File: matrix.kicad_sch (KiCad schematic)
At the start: 166 parts

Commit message: arcade session 3
added footprints; lots of errors :( problem for next time i am free
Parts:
- D10, D11, D12, D13, D14, D15, D16, D17, D18, D19, D2, D20, D21, D22, D23, D24, D25, D26, D27, D28, D29, D3, D30, D31, D32, D33, D34, D35, D36, D37, D38, D39, D4, D40, D41, D42, D43, D44, D45, D46, D47, D48, D49, D5, D50, D51, D52, D53, D54, D55, D56, D57, D58, D59, D6, D60, D61, D62, D63, D64, D65, D66, D67, D68, D69, D7, D70, D71, D72, D73, D74, D75, D76, D77, D78, D79, D8, D80, D81, D82, D83, D84, D9: footprint (none) -> Diode_SMD:D_SOD-123
- MX29: footprint PCM_marbastlib-mx:SW_MX_HS_CPG151101S11_1u -> PCM_marbastlib-mx:STAB_MX_2u
- MX31, MX44: footprint PCM_marbastlib-mx:SW_MX_HS_CPG151101S11_1u -> PCM_marbastlib-mx:SW_MX_HS_CPG151101S11_1.5u
- MX46, MX71: footprint PCM_marbastlib-mx:SW_MX_HS_CPG151101S11_1u -> PCM_marbastlib-mx:SW_MX_HS_CPG151101S11_1.75u
- MX58, MX60: footprint PCM_marbastlib-mx:SW_MX_HS_CPG151101S11_1u -> PCM_marbastlib-mx:STAB_MX_2.25u
- MX74, MX75, MX76: footprint PCM_marbastlib-mx:SW_MX_HS_CPG151101S11_1u -> PCM_marbastlib-mx:SW_MX_HS_CPG151101S11_1.25u
- MX77: footprint PCM_marbastlib-mx:SW_MX_HS_CPG151101S11_1u -> PCM_marbastlib-mx:STAB_MX_6.25u

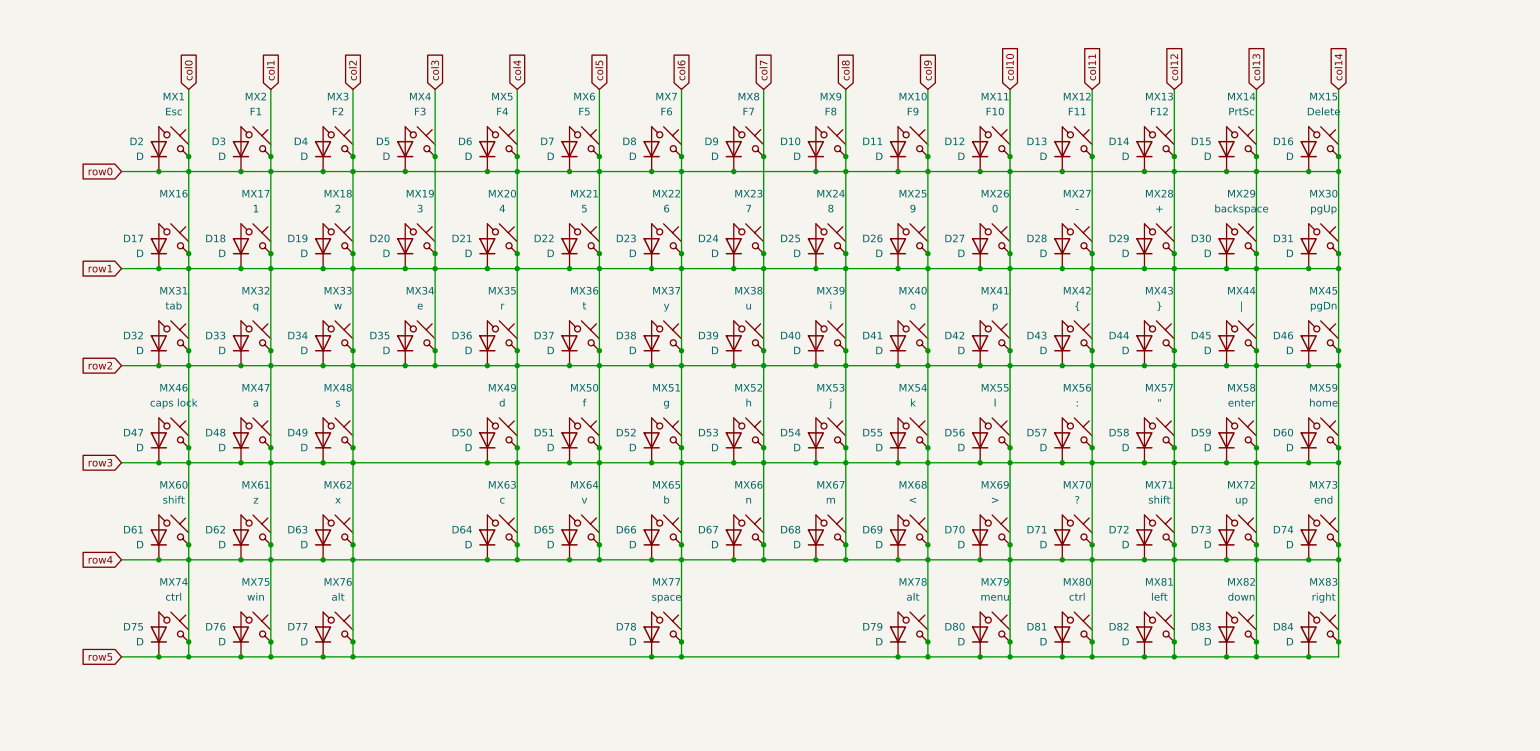
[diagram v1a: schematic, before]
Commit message: arcade session 4(?)
footprints fixed and components placed/pcb editor settings set up
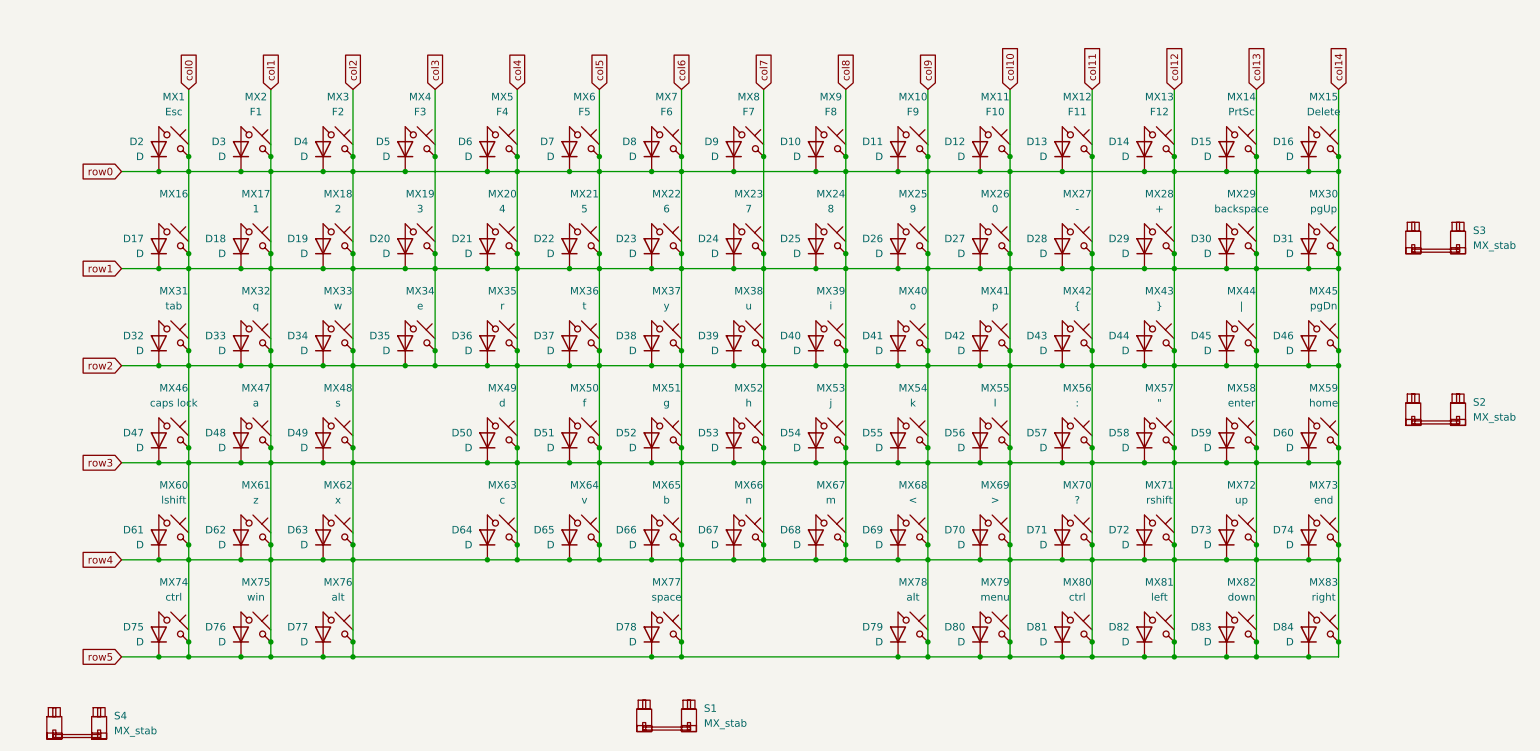
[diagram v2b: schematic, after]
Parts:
- added S1: MX_stab, PCM_marbastlib-mx:STAB_MX_P_6.25u, symbol PCM_marbastlib-mx:MX_stab
- added S2, S4: MX_stab, PCM_marbastlib-mx:STAB_MX_2u, symbol PCM_marbastlib-mx:MX_stab
- added S3: MX_stab, PCM_marbastlib-mx:STAB_MX_P_2u, symbol PCM_marbastlib-mx:MX_stab
- MX29: footprint PCM_marbastlib-mx:STAB_MX_2u -> PCM_marbastlib-mx:SW_MX_HS_CPG151101S11_1u
- MX31, MX44: footprint PCM_marbastlib-mx:SW_MX_HS_CPG151101S11_1.5u -> PCM_marbastlib-mx:SW_MX_HS_CPG151101S11_1u
- MX46: footprint PCM_marbastlib-mx:SW_MX_HS_CPG151101S11_1.75u -> PCM_marbastlib-mx:SW_MX_HS_CPG151101S11_1u
- MX58: footprint PCM_marbastlib-mx:STAB_MX_2.25u -> PCM_marbastlib-mx:SW_MX_HS_CPG151101S11_1u
- MX60: value shift -> lshift; footprint PCM_marbastlib-mx:STAB_MX_2.25u -> PCM_marbastlib-mx:SW_MX_HS_CPG151101S11_1u
- MX71: value shift -> rshift; footprint PCM_marbastlib-mx:SW_MX_HS_CPG151101S11_1.75u -> PCM_marbastlib-mx:SW_MX_HS_CPG151101S11_1u
- MX74, MX75, MX76: footprint PCM_marbastlib-mx:SW_MX_HS_CPG151101S11_1.25u -> PCM_marbastlib-mx:SW_MX_HS_CPG151101S11_1u
- MX77: footprint PCM_marbastlib-mx:STAB_MX_6.25u -> PCM_marbastlib-mx:SW_MX_HS_CPG151101S11_1u

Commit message: fixed mistakes
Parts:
- removed MX1: Esc, PCM_marbastlib-mx:SW_MX_HS_CPG151101S11_1u, symbol PCM_marbastlib-mx:MX_SW_HS_CPG151101S11
- removed MX10: F9, PCM_marbastlib-mx:SW_MX_HS_CPG151101S11_1u, symbol PCM_marbastlib-mx:MX_SW_HS_CPG151101S11
- removed MX11: F10, PCM_marbastlib-mx:SW_MX_HS_CPG151101S11_1u, symbol PCM_marbastlib-mx:MX_SW_HS_CPG151101S11
- removed MX12: F11, PCM_marbastlib-mx:SW_MX_HS_CPG151101S11_1u, symbol PCM_marbastlib-mx:MX_SW_HS_CPG151101S11
- removed MX13: F12, PCM_marbastlib-mx:SW_MX_HS_CPG151101S11_1u, symbol PCM_marbastlib-mx:MX_SW_HS_CPG151101S11
- removed MX14: PrtSc, PCM_marbastlib-mx:SW_MX_HS_CPG151101S11_1u, symbol PCM_marbastlib-mx:MX_SW_HS_CPG151101S11
- removed MX15: Delete, PCM_marbastlib-mx:SW_MX_HS_CPG151101S11_1u, symbol PCM_marbastlib-mx:MX_SW_HS_CPG151101S11
- removed MX16: ~, PCM_marbastlib-mx:SW_MX_HS_CPG151101S11_1u, symbol PCM_marbastlib-mx:MX_SW_HS_CPG151101S11
- removed MX17: 1, PCM_marbastlib-mx:SW_MX_HS_CPG151101S11_1u, symbol PCM_marbastlib-mx:MX_SW_HS_CPG151101S11
- removed MX18: 2, PCM_marbastlib-mx:SW_MX_HS_CPG151101S11_1u, symbol PCM_marbastlib-mx:MX_SW_HS_CPG151101S11
- removed MX19: 3, PCM_marbastlib-mx:SW_MX_HS_CPG151101S11_1u, symbol PCM_marbastlib-mx:MX_SW_HS_CPG151101S11
- removed MX2: F1, PCM_marbastlib-mx:SW_MX_HS_CPG151101S11_1u, symbol PCM_marbastlib-mx:MX_SW_HS_CPG151101S11
- removed MX20: 4, PCM_marbastlib-mx:SW_MX_HS_CPG151101S11_1u, symbol PCM_marbastlib-mx:MX_SW_HS_CPG151101S11
- removed MX21: 5, PCM_marbastlib-mx:SW_MX_HS_CPG151101S11_1u, symbol PCM_marbastlib-mx:MX_SW_HS_CPG151101S11
- removed MX22: 6, PCM_marbastlib-mx:SW_MX_HS_CPG151101S11_1u, symbol PCM_marbastlib-mx:MX_SW_HS_CPG151101S11
- removed MX23: 7, PCM_marbastlib-mx:SW_MX_HS_CPG151101S11_1u, symbol PCM_marbastlib-mx:MX_SW_HS_CPG151101S11
- removed MX24: 8, PCM_marbastlib-mx:SW_MX_HS_CPG151101S11_1u, symbol PCM_marbastlib-mx:MX_SW_HS_CPG151101S11
- removed MX25: 9, PCM_marbastlib-mx:SW_MX_HS_CPG151101S11_1u, symbol PCM_marbastlib-mx:MX_SW_HS_CPG151101S11
- removed MX26: 0, PCM_marbastlib-mx:SW_MX_HS_CPG151101S11_1u, symbol PCM_marbastlib-mx:MX_SW_HS_CPG151101S11
- removed MX27: -, PCM_marbastlib-mx:SW_MX_HS_CPG151101S11_1u, symbol PCM_marbastlib-mx:MX_SW_HS_CPG151101S11
- removed MX28: +, PCM_marbastlib-mx:SW_MX_HS_CPG151101S11_1u, symbol PCM_marbastlib-mx:MX_SW_HS_CPG151101S11
- removed MX29: backspace, PCM_marbastlib-mx:SW_MX_HS_CPG151101S11_1u, symbol PCM_marbastlib-mx:MX_SW_HS_CPG151101S11
- removed MX3: F2, PCM_marbastlib-mx:SW_MX_HS_CPG151101S11_1u, symbol PCM_marbastlib-mx:MX_SW_HS_CPG151101S11
- removed MX30: pgUp, PCM_marbastlib-mx:SW_MX_HS_CPG151101S11_1u, symbol PCM_marbastlib-mx:MX_SW_HS_CPG151101S11
- removed MX31: tab, PCM_marbastlib-mx:SW_MX_HS_CPG151101S11_1u, symbol PCM_marbastlib-mx:MX_SW_HS_CPG151101S11
- removed MX32: q, PCM_marbastlib-mx:SW_MX_HS_CPG151101S11_1u, symbol PCM_marbastlib-mx:MX_SW_HS_CPG151101S11
- removed MX33: w, PCM_marbastlib-mx:SW_MX_HS_CPG151101S11_1u, symbol PCM_marbastlib-mx:MX_SW_HS_CPG151101S11
- removed MX34: e, PCM_marbastlib-mx:SW_MX_HS_CPG151101S11_1u, symbol PCM_marbastlib-mx:MX_SW_HS_CPG151101S11
- removed MX35: r, PCM_marbastlib-mx:SW_MX_HS_CPG151101S11_1u, symbol PCM_marbastlib-mx:MX_SW_HS_CPG151101S11
- removed MX36: t, PCM_marbastlib-mx:SW_MX_HS_CPG151101S11_1u, symbol PCM_marbastlib-mx:MX_SW_HS_CPG151101S11
- removed MX37: y, PCM_marbastlib-mx:SW_MX_HS_CPG151101S11_1u, symbol PCM_marbastlib-mx:MX_SW_HS_CPG151101S11
- removed MX38: u, PCM_marbastlib-mx:SW_MX_HS_CPG151101S11_1u, symbol PCM_marbastlib-mx:MX_SW_HS_CPG151101S11
- removed MX39: i, PCM_marbastlib-mx:SW_MX_HS_CPG151101S11_1u, symbol PCM_marbastlib-mx:MX_SW_HS_CPG151101S11
- removed MX4: F3, PCM_marbastlib-mx:SW_MX_HS_CPG151101S11_1u, symbol PCM_marbastlib-mx:MX_SW_HS_CPG151101S11
- removed MX40: o, PCM_marbastlib-mx:SW_MX_HS_CPG151101S11_1u, symbol PCM_marbastlib-mx:MX_SW_HS_CPG151101S11
- removed MX41: p, PCM_marbastlib-mx:SW_MX_HS_CPG151101S11_1u, symbol PCM_marbastlib-mx:MX_SW_HS_CPG151101S11
- removed MX42: {, PCM_marbastlib-mx:SW_MX_HS_CPG151101S11_1u, symbol PCM_marbastlib-mx:MX_SW_HS_CPG151101S11
- removed MX43: }, PCM_marbastlib-mx:SW_MX_HS_CPG151101S11_1u, symbol PCM_marbastlib-mx:MX_SW_HS_CPG151101S11
- removed MX44: |, PCM_marbastlib-mx:SW_MX_HS_CPG151101S11_1u, symbol PCM_marbastlib-mx:MX_SW_HS_CPG151101S11
- removed MX45: pgDn, PCM_marbastlib-mx:SW_MX_HS_CPG151101S11_1u, symbol PCM_marbastlib-mx:MX_SW_HS_CPG151101S11
- removed MX46: caps lock, PCM_marbastlib-mx:SW_MX_HS_CPG151101S11_1u, symbol PCM_marbastlib-mx:MX_SW_HS_CPG151101S11
- removed MX47: a, PCM_marbastlib-mx:SW_MX_HS_CPG151101S11_1u, symbol PCM_marbastlib-mx:MX_SW_HS_CPG151101S11
- removed MX48: s, PCM_marbastlib-mx:SW_MX_HS_CPG151101S11_1u, symbol PCM_marbastlib-mx:MX_SW_HS_CPG151101S11
- removed MX49: d, PCM_marbastlib-mx:SW_MX_HS_CPG151101S11_1u, symbol PCM_marbastlib-mx:MX_SW_HS_CPG151101S11
- removed MX5: F4, PCM_marbastlib-mx:SW_MX_HS_CPG151101S11_1u, symbol PCM_marbastlib-mx:MX_SW_HS_CPG151101S11
- removed MX50: f, PCM_marbastlib-mx:SW_MX_HS_CPG151101S11_1u, symbol PCM_marbastlib-mx:MX_SW_HS_CPG151101S11
- removed MX51: g, PCM_marbastlib-mx:SW_MX_HS_CPG151101S11_1u, symbol PCM_marbastlib-mx:MX_SW_HS_CPG151101S11
- removed MX52: h, PCM_marbastlib-mx:SW_MX_HS_CPG151101S11_1u, symbol PCM_marbastlib-mx:MX_SW_HS_CPG151101S11
- removed MX53: j, PCM_marbastlib-mx:SW_MX_HS_CPG151101S11_1u, symbol PCM_marbastlib-mx:MX_SW_HS_CPG151101S11
- removed MX54: k, PCM_marbastlib-mx:SW_MX_HS_CPG151101S11_1u, symbol PCM_marbastlib-mx:MX_SW_HS_CPG151101S11
- removed MX55: l, PCM_marbastlib-mx:SW_MX_HS_CPG151101S11_1u, symbol PCM_marbastlib-mx:MX_SW_HS_CPG151101S11
- removed MX56: :, PCM_marbastlib-mx:SW_MX_HS_CPG151101S11_1u, symbol PCM_marbastlib-mx:MX_SW_HS_CPG151101S11
- removed MX57: ", PCM_marbastlib-mx:SW_MX_HS_CPG151101S11_1u, symbol PCM_marbastlib-mx:MX_SW_HS_CPG151101S11
- removed MX58: enter, PCM_marbastlib-mx:SW_MX_HS_CPG151101S11_1u, symbol PCM_marbastlib-mx:MX_SW_HS_CPG151101S11
- removed MX59: home, PCM_marbastlib-mx:SW_MX_HS_CPG151101S11_1u, symbol PCM_marbastlib-mx:MX_SW_HS_CPG151101S11
- removed MX6: F5, PCM_marbastlib-mx:SW_MX_HS_CPG151101S11_1u, symbol PCM_marbastlib-mx:MX_SW_HS_CPG151101S11
- removed MX60: lshift, PCM_marbastlib-mx:SW_MX_HS_CPG151101S11_1u, symbol PCM_marbastlib-mx:MX_SW_HS_CPG151101S11
- removed MX61: z, PCM_marbastlib-mx:SW_MX_HS_CPG151101S11_1u, symbol PCM_marbastlib-mx:MX_SW_HS_CPG151101S11
- removed MX62: x, PCM_marbastlib-mx:SW_MX_HS_CPG151101S11_1u, symbol PCM_marbastlib-mx:MX_SW_HS_CPG151101S11
- removed MX63: c, PCM_marbastlib-mx:SW_MX_HS_CPG151101S11_1u, symbol PCM_marbastlib-mx:MX_SW_HS_CPG151101S11
- removed MX64: v, PCM_marbastlib-mx:SW_MX_HS_CPG151101S11_1u, symbol PCM_marbastlib-mx:MX_SW_HS_CPG151101S11
- removed MX65: b, PCM_marbastlib-mx:SW_MX_HS_CPG151101S11_1u, symbol PCM_marbastlib-mx:MX_SW_HS_CPG151101S11
- removed MX66: n, PCM_marbastlib-mx:SW_MX_HS_CPG151101S11_1u, symbol PCM_marbastlib-mx:MX_SW_HS_CPG151101S11
- removed MX67: m, PCM_marbastlib-mx:SW_MX_HS_CPG151101S11_1u, symbol PCM_marbastlib-mx:MX_SW_HS_CPG151101S11
- removed MX68: <, PCM_marbastlib-mx:SW_MX_HS_CPG151101S11_1u, symbol PCM_marbastlib-mx:MX_SW_HS_CPG151101S11
- removed MX69: >, PCM_marbastlib-mx:SW_MX_HS_CPG151101S11_1u, symbol PCM_marbastlib-mx:MX_SW_HS_CPG151101S11
- removed MX7: F6, PCM_marbastlib-mx:SW_MX_HS_CPG151101S11_1u, symbol PCM_marbastlib-mx:MX_SW_HS_CPG151101S11
- removed MX70: ?, PCM_marbastlib-mx:SW_MX_HS_CPG151101S11_1u, symbol PCM_marbastlib-mx:MX_SW_HS_CPG151101S11
- removed MX71: rshift, PCM_marbastlib-mx:SW_MX_HS_CPG151101S11_1u, symbol PCM_marbastlib-mx:MX_SW_HS_CPG151101S11
- removed MX72: up, PCM_marbastlib-mx:SW_MX_HS_CPG151101S11_1u, symbol PCM_marbastlib-mx:MX_SW_HS_CPG151101S11
- removed MX73: end, PCM_marbastlib-mx:SW_MX_HS_CPG151101S11_1u, symbol PCM_marbastlib-mx:MX_SW_HS_CPG151101S11
- removed MX74, MX80: ctrl, PCM_marbastlib-mx:SW_MX_HS_CPG151101S11_1u, symbol PCM_marbastlib-mx:MX_SW_HS_CPG151101S11
- removed MX75: win, PCM_marbastlib-mx:SW_MX_HS_CPG151101S11_1u, symbol PCM_marbastlib-mx:MX_SW_HS_CPG151101S11
- removed MX76, MX78: alt, PCM_marbastlib-mx:SW_MX_HS_CPG151101S11_1u, symbol PCM_marbastlib-mx:MX_SW_HS_CPG151101S11
- removed MX77: space, PCM_marbastlib-mx:SW_MX_HS_CPG151101S11_1u, symbol PCM_marbastlib-mx:MX_SW_HS_CPG151101S11
- removed MX79: menu, PCM_marbastlib-mx:SW_MX_HS_CPG151101S11_1u, symbol PCM_marbastlib-mx:MX_SW_HS_CPG151101S11
- removed MX8: F7, PCM_marbastlib-mx:SW_MX_HS_CPG151101S11_1u, symbol PCM_marbastlib-mx:MX_SW_HS_CPG151101S11
- removed MX81: left, PCM_marbastlib-mx:SW_MX_HS_CPG151101S11_1u, symbol PCM_marbastlib-mx:MX_SW_HS_CPG151101S11
- removed MX82: down, PCM_marbastlib-mx:SW_MX_HS_CPG151101S11_1u, symbol PCM_marbastlib-mx:MX_SW_HS_CPG151101S11
- removed MX83: right, PCM_marbastlib-mx:SW_MX_HS_CPG151101S11_1u, symbol PCM_marbastlib-mx:MX_SW_HS_CPG151101S11
- removed MX9: F8, PCM_marbastlib-mx:SW_MX_HS_CPG151101S11_1u, symbol PCM_marbastlib-mx:MX_SW_HS_CPG151101S11
- removed S1: MX_stab, PCM_marbastlib-mx:STAB_MX_P_6.25u, symbol PCM_marbastlib-mx:MX_stab
- removed S2, S4: MX_stab, PCM_marbastlib-mx:STAB_MX_2u, symbol PCM_marbastlib-mx:MX_stab
- removed S3: MX_stab, PCM_marbastlib-mx:STAB_MX_P_2u, symbol PCM_marbastlib-mx:MX_stab
- added MX1: esc, MX_Alps_Hybrid:MX-Alps-Hybrid-1U, symbol PCM_marbastlib-mx:MX_SW_solder
- added MX10: f9, MX_Alps_Hybrid:MX-Alps-Hybrid-1U, symbol PCM_marbastlib-mx:MX_SW_solder
- added MX11: f10, MX_Alps_Hybrid:MX-Alps-Hybrid-1U, symbol PCM_marbastlib-mx:MX_SW_solder
- added MX12: f11, MX_Alps_Hybrid:MX-Alps-Hybrid-1U, symbol PCM_marbastlib-mx:MX_SW_solder
- added MX13: f12, MX_Alps_Hybrid:MX-Alps-Hybrid-1U, symbol PCM_marbastlib-mx:MX_SW_solder
- added MX14: prtsc, MX_Alps_Hybrid:MX-Alps-Hybrid-1U, symbol PCM_marbastlib-mx:MX_SW_solder
- added MX15: del, MX_Alps_Hybrid:MX-Alps-Hybrid-1U, symbol PCM_marbastlib-mx:MX_SW_solder
- added MX16: ~, MX_Alps_Hybrid:MX-Alps-Hybrid-1U, symbol PCM_marbastlib-mx:MX_SW_solder
- added MX17: 1, MX_Alps_Hybrid:MX-Alps-Hybrid-1U, symbol PCM_marbastlib-mx:MX_SW_solder
- added MX18: 2, MX_Alps_Hybrid:MX-Alps-Hybrid-1U, symbol PCM_marbastlib-mx:MX_SW_solder
- added MX19: 3, MX_Alps_Hybrid:MX-Alps-Hybrid-1U, symbol PCM_marbastlib-mx:MX_SW_solder
- added MX2: f1, MX_Alps_Hybrid:MX-Alps-Hybrid-1U, symbol PCM_marbastlib-mx:MX_SW_solder
- added MX20: 4, MX_Alps_Hybrid:MX-Alps-Hybrid-1U, symbol PCM_marbastlib-mx:MX_SW_solder
- added MX21: 5, MX_Alps_Hybrid:MX-Alps-Hybrid-1U, symbol PCM_marbastlib-mx:MX_SW_solder
- added MX22: 6, MX_Alps_Hybrid:MX-Alps-Hybrid-1U, symbol PCM_marbastlib-mx:MX_SW_solder
- added MX23: 7, MX_Alps_Hybrid:MX-Alps-Hybrid-1U, symbol PCM_marbastlib-mx:MX_SW_solder
- added MX24: 8, MX_Alps_Hybrid:MX-Alps-Hybrid-1U, symbol PCM_marbastlib-mx:MX_SW_solder
- added MX25: 9, MX_Alps_Hybrid:MX-Alps-Hybrid-1U, symbol PCM_marbastlib-mx:MX_SW_solder
- added MX26: 0, MX_Alps_Hybrid:MX-Alps-Hybrid-1U, symbol PCM_marbastlib-mx:MX_SW_solder
- added MX27: -, MX_Alps_Hybrid:MX-Alps-Hybrid-1U, symbol PCM_marbastlib-mx:MX_SW_solder
- added MX28: =, MX_Alps_Hybrid:MX-Alps-Hybrid-1U, symbol PCM_marbastlib-mx:MX_SW_solder
- added MX29: backspace, MX_Alps_Hybrid:MX-Alps-Hybrid-2U-ReversedStabilizers, symbol PCM_marbastlib-mx:MX_SW_solder
- added MX3: f2, MX_Alps_Hybrid:MX-Alps-Hybrid-1U, symbol PCM_marbastlib-mx:MX_SW_solder
- added MX30: pgup, MX_Alps_Hybrid:MX-Alps-Hybrid-1U, symbol PCM_marbastlib-mx:MX_SW_solder
- added MX31: tab, MX_Alps_Hybrid:MX-Alps-Hybrid-1.5U, symbol PCM_marbastlib-mx:MX_SW_solder
- added MX32: q, MX_Alps_Hybrid:MX-Alps-Hybrid-1U, symbol PCM_marbastlib-mx:MX_SW_solder
- added MX33: w, MX_Alps_Hybrid:MX-Alps-Hybrid-1U, symbol PCM_marbastlib-mx:MX_SW_solder
- added MX34: e, MX_Alps_Hybrid:MX-Alps-Hybrid-1U, symbol PCM_marbastlib-mx:MX_SW_solder
- added MX35: r, MX_Alps_Hybrid:MX-Alps-Hybrid-1U, symbol PCM_marbastlib-mx:MX_SW_solder
- added MX36: t, MX_Alps_Hybrid:MX-Alps-Hybrid-1U, symbol PCM_marbastlib-mx:MX_SW_solder
- added MX37: y, MX_Alps_Hybrid:MX-Alps-Hybrid-1U, symbol PCM_marbastlib-mx:MX_SW_solder
- added MX38: u, MX_Alps_Hybrid:MX-Alps-Hybrid-1U, symbol PCM_marbastlib-mx:MX_SW_solder
- added MX39: i, MX_Alps_Hybrid:MX-Alps-Hybrid-1U, symbol PCM_marbastlib-mx:MX_SW_solder
- added MX4: f3, MX_Alps_Hybrid:MX-Alps-Hybrid-1U, symbol PCM_marbastlib-mx:MX_SW_solder
- added MX40: o, MX_Alps_Hybrid:MX-Alps-Hybrid-1U, symbol PCM_marbastlib-mx:MX_SW_solder
- added MX41: p, MX_Alps_Hybrid:MX-Alps-Hybrid-1U, symbol PCM_marbastlib-mx:MX_SW_solder
- added MX42: [, MX_Alps_Hybrid:MX-Alps-Hybrid-1U, symbol PCM_marbastlib-mx:MX_SW_solder
- added MX43: ], MX_Alps_Hybrid:MX-Alps-Hybrid-1U, symbol PCM_marbastlib-mx:MX_SW_solder
- added MX44: \, MX_Alps_Hybrid:MX-Alps-Hybrid-1.5U, symbol PCM_marbastlib-mx:MX_SW_solder
- added MX45: pgdn, MX_Alps_Hybrid:MX-Alps-Hybrid-1U, symbol PCM_marbastlib-mx:MX_SW_solder
- added MX46: caps lock, MX_Alps_Hybrid:MX-Alps-Hybrid-1.75U, symbol PCM_marbastlib-mx:MX_SW_solder
- added MX47: a, MX_Alps_Hybrid:MX-Alps-Hybrid-1U, symbol PCM_marbastlib-mx:MX_SW_solder
- added MX48: s, MX_Alps_Hybrid:MX-Alps-Hybrid-1U, symbol PCM_marbastlib-mx:MX_SW_solder
- added MX49: d, MX_Alps_Hybrid:MX-Alps-Hybrid-1U, symbol PCM_marbastlib-mx:MX_SW_solder
- added MX5: f4, MX_Alps_Hybrid:MX-Alps-Hybrid-1U, symbol PCM_marbastlib-mx:MX_SW_solder
- added MX50: f, MX_Alps_Hybrid:MX-Alps-Hybrid-1U, symbol PCM_marbastlib-mx:MX_SW_solder
- added MX51: g, MX_Alps_Hybrid:MX-Alps-Hybrid-1U, symbol PCM_marbastlib-mx:MX_SW_solder
- added MX52: h, MX_Alps_Hybrid:MX-Alps-Hybrid-1U, symbol PCM_marbastlib-mx:MX_SW_solder
- added MX53: j, MX_Alps_Hybrid:MX-Alps-Hybrid-1U, symbol PCM_marbastlib-mx:MX_SW_solder
- added MX54: k, MX_Alps_Hybrid:MX-Alps-Hybrid-1U, symbol PCM_marbastlib-mx:MX_SW_solder
- added MX55: l, MX_Alps_Hybrid:MX-Alps-Hybrid-1U, symbol PCM_marbastlib-mx:MX_SW_solder
- added MX56: ;, MX_Alps_Hybrid:MX-Alps-Hybrid-1U, symbol PCM_marbastlib-mx:MX_SW_solder
- added MX57: ', MX_Alps_Hybrid:MX-Alps-Hybrid-1U, symbol PCM_marbastlib-mx:MX_SW_solder
- added MX58: enter, MX_Alps_Hybrid:MX-Alps-Hybrid-2.25U-ReversedStabilizers, symbol PCM_marbastlib-mx:MX_SW_solder
- added MX59: home, MX_Alps_Hybrid:MX-Alps-Hybrid-1U, symbol PCM_marbastlib-mx:MX_SW_solder
- added MX6: f5, MX_Alps_Hybrid:MX-Alps-Hybrid-1U, symbol PCM_marbastlib-mx:MX_SW_solder
- added MX60: lshift, MX_Alps_Hybrid:MX-Alps-Hybrid-2.25U-ReversedStabilizers, symbol PCM_marbastlib-mx:MX_SW_solder
- added MX61: z, MX_Alps_Hybrid:MX-Alps-Hybrid-1U, symbol PCM_marbastlib-mx:MX_SW_solder
- added MX62: x, MX_Alps_Hybrid:MX-Alps-Hybrid-1U, symbol PCM_marbastlib-mx:MX_SW_solder
- added MX63: c, MX_Alps_Hybrid:MX-Alps-Hybrid-1U, symbol PCM_marbastlib-mx:MX_SW_solder
- added MX64: v, MX_Alps_Hybrid:MX-Alps-Hybrid-1U, symbol PCM_marbastlib-mx:MX_SW_solder
- added MX65: b, MX_Alps_Hybrid:MX-Alps-Hybrid-1U, symbol PCM_marbastlib-mx:MX_SW_solder
- added MX66: n, MX_Alps_Hybrid:MX-Alps-Hybrid-1U, symbol PCM_marbastlib-mx:MX_SW_solder
- added MX67: m, MX_Alps_Hybrid:MX-Alps-Hybrid-1U, symbol PCM_marbastlib-mx:MX_SW_solder
- added MX68: ,, MX_Alps_Hybrid:MX-Alps-Hybrid-1U, symbol PCM_marbastlib-mx:MX_SW_solder
- added MX69: ., MX_Alps_Hybrid:MX-Alps-Hybrid-1U, symbol PCM_marbastlib-mx:MX_SW_solder
- added MX7: f6, MX_Alps_Hybrid:MX-Alps-Hybrid-1U, symbol PCM_marbastlib-mx:MX_SW_solder
- added MX70: /, MX_Alps_Hybrid:MX-Alps-Hybrid-1U, symbol PCM_marbastlib-mx:MX_SW_solder
- added MX71: rshift, MX_Alps_Hybrid:MX-Alps-Hybrid-1.75U, symbol PCM_marbastlib-mx:MX_SW_solder
- added MX72: up, MX_Alps_Hybrid:MX-Alps-Hybrid-1U, symbol PCM_marbastlib-mx:MX_SW_solder
- added MX73: end, MX_Alps_Hybrid:MX-Alps-Hybrid-1U, symbol PCM_marbastlib-mx:MX_SW_solder
- added MX74: ctrl, MX_Alps_Hybrid:MX-Alps-Hybrid-1.25U, symbol PCM_marbastlib-mx:MX_SW_solder
- added MX75: win, MX_Alps_Hybrid:MX-Alps-Hybrid-1.25U, symbol PCM_marbastlib-mx:MX_SW_solder
- added MX76: alt, MX_Alps_Hybrid:MX-Alps-Hybrid-1.25U, symbol PCM_marbastlib-mx:MX_SW_solder
- added MX77: space, MX_Alps_Hybrid:MX-Alps-Hybrid-6.25U-ReversedStabilizers, symbol PCM_marbastlib-mx:MX_SW_solder
- added MX78: alt, MX_Alps_Hybrid:MX-Alps-Hybrid-1U, symbol PCM_marbastlib-mx:MX_SW_solder
- added MX79: menu, MX_Alps_Hybrid:MX-Alps-Hybrid-1U, symbol PCM_marbastlib-mx:MX_SW_solder
- added MX8: f7, MX_Alps_Hybrid:MX-Alps-Hybrid-1U, symbol PCM_marbastlib-mx:MX_SW_solder
- added MX80: ctrl, MX_Alps_Hybrid:MX-Alps-Hybrid-1U, symbol PCM_marbastlib-mx:MX_SW_solder
- added MX81: left, MX_Alps_Hybrid:MX-Alps-Hybrid-1U, symbol PCM_marbastlib-mx:MX_SW_solder
- added MX82: bottom, MX_Alps_Hybrid:MX-Alps-Hybrid-1U, symbol PCM_marbastlib-mx:MX_SW_solder
- added MX83: right, MX_Alps_Hybrid:MX-Alps-Hybrid-1U, symbol PCM_marbastlib-mx:MX_SW_solder
- added MX9: f8, MX_Alps_Hybrid:MX-Alps-Hybrid-1U, symbol PCM_marbastlib-mx:MX_SW_solder
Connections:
- net col0: now also MX1.2, MX16.2, MX31.2, MX46.2, MX60.2, MX74.2; no longer D10.1 (K), D11.1 (K), D12.1 (K), D13.1 (K), D14.1 (K), D15.1 (K), D16.1 (K), D17.1 (K), D18.1 (K), D19.1 (K), D2.1 (K), D20.1 (K), D21.1 (K), D22.1 (K), D23.1 (K), D24.1 (K), D25.1 (K), D26.1 (K), D27.1 (K), D28.1 (K), D29.1 (K), D3.1 (K), D30.1 (K), D31.1 (K), D32.1 (K), D33.1 (K), D34.1 (K), D35.1 (K), D36.1 (K), D37.1 (K), D38.1 (K), D39.1 (K), D4.1 (K), D40.1 (K), D41.1 (K), D42.1 (K), D43.1 (K), D44.1 (K), D45.1 (K), D46.1 (K), D47.1 (K), D48.1 (K), D49.1 (K), D5.1 (K), D50.1 (K), D51.1 (K), D52.1 (K), D53.1 (K), D54.1 (K), D55.1 (K), D56.1 (K), D57.1 (K), D58.1 (K), D59.1 (K), D6.1 (K), D60.1 (K), D61.1 (K), D62.1 (K), D63.1 (K), D64.1 (K), D65.1 (K), D66.1 (K), D67.1 (K), D68.1 (K), D69.1 (K), D7.1 (K), D70.1 (K), D71.1 (K), D72.1 (K), D73.1 (K), D74.1 (K), D75.1 (K), D76.1 (K), D77.1 (K), D78.1 (K), D79.1 (K), D8.1 (K), D80.1 (K), D81.1 (K), D82.1 (K), D83.1 (K), D84.1 (K), D9.1 (K)
- net at D8.2 (A): now also MX7.1
- net at D61.2 (A): now also MX60.1
- net at D81.2 (A): now also MX80.1
- net at D9.2 (A): now also MX8.1
- net at D17.2 (A): now also MX16.1
- net at D63.2 (A): now also MX62.1
- net at D83.2 (A): now also MX82.1
- net at D69.2 (A): now also MX68.1
- net at D79.2 (A): now also MX78.1
- net at D78.2 (A): now also MX77.1
- net at D58.2 (A): now also MX57.1
- net at D25.2 (A): now also MX24.1
- net at D31.2 (A): now also MX30.1
- net at D37.2 (A): now also MX36.1
- net at D54.2 (A): now also MX53.1
- net at D73.2 (A): now also MX72.1
- net at D51.2 (A): now also MX50.1
- net at D76.2 (A): now also MX75.1
- net at D4.2 (A): now also MX3.1
- net at D30.2 (A): now also MX29.1
- net at D7.2 (A): now also MX6.1
- net at D45.2 (A): now also MX44.1
- net at D39.2 (A): now also MX38.1
- net at D5.2 (A): now also MX4.1
- net at D32.2 (A): now also MX31.1
- net at D72.2 (A): now also MX71.1
- net at D48.2 (A): now also MX47.1
- net at D13.2 (A): now also MX12.1
- net at D3.2 (A): now also MX2.1
- net at D21.2 (A): now also MX20.1
- net at D46.2 (A): now also MX45.1
- net at D43.2 (A): now also MX42.1
- net at D80.2 (A): now also MX79.1
- net at D74.2 (A): now also MX73.1
- net at D68.2 (A): now also MX67.1
- net at D19.2 (A): now also MX18.1
- net at D71.2 (A): now also MX70.1
- net at D82.2 (A): now also MX81.1
- net at D40.2 (A): now also MX39.1
- net at D47.2 (A): now also MX46.1
- net at D60.2 (A): now also MX59.1
- net at D50.2 (A): now also MX49.1
- net at D20.2 (A): now also MX19.1
- net at D26.2 (A): now also MX25.1
- net at D27.2 (A): now also MX26.1
- net at D84.2 (A): now also MX83.1
- net at D55.2 (A): now also MX54.1
- net at D49.2 (A): now also MX48.1
- net at D42.2 (A): now also MX41.1
- net at D10.2 (A): now also MX9.1
- net at D57.2 (A): now also MX56.1
- net at D14.2 (A): now also MX13.1
- net at D29.2 (A): now also MX28.1
- net at D65.2 (A): now also MX64.1
- net at D15.2 (A): now also MX14.1
- net at D67.2 (A): now also MX66.1
- net at D36.2 (A): now also MX35.1
- net at D35.2 (A): now also MX34.1
- net at D52.2 (A): now also MX51.1
- net at D6.2 (A): now also MX5.1
- net at D11.2 (A): now also MX10.1
- net at D70.2 (A): now also MX69.1
- net at D41.2 (A): now also MX40.1
- net at D62.2 (A): now also MX61.1
- net at D56.2 (A): now also MX55.1
- net at D38.2 (A): now also MX37.1
- net at D24.2 (A): now also MX23.1
- net at D66.2 (A): now also MX65.1
- net at D77.2 (A): now also MX76.1
- net at D2.2 (A): now also MX1.1
- net at D75.2 (A): now also MX74.1
- net at D64.2 (A): now also MX63.1
- net at D28.2 (A): now also MX27.1
- net at D18.2 (A): now also MX17.1
- net at D44.2 (A): now also MX43.1
- net at D23.2 (A): now also MX22.1
- net at D22.2 (A): now also MX21.1
- net at D34.2 (A): now also MX33.1
- net at D53.2 (A): now also MX52.1
- net at D33.2 (A): now also MX32.1
- net at D59.2 (A): now also MX58.1
- net at D12.2 (A): now also MX11.1
- net at D16.2 (A): now also MX15.1
- new net col1: MX17.2, MX2.2, MX32.2, MX47.2, MX61.2, MX75.2
- new net col10: MX11.2, MX26.2, MX41.2, MX55.2, MX69.2, MX79.2
- new net col11: MX12.2, MX27.2, MX42.2, MX56.2, MX70.2, MX80.2
- new net col12: MX13.2, MX28.2, MX43.2, MX57.2, MX71.2, MX81.2
- new net col13: MX14.2, MX29.2, MX44.2, MX58.2, MX72.2, MX82.2
- new net col14: MX15.2, MX30.2, MX45.2, MX59.2, MX73.2, MX83.2
- new net col2: MX18.2, MX3.2, MX33.2, MX48.2, MX62.2, MX76.2
- new net col3: MX19.2, MX34.2, MX4.2
- new net col4: MX20.2, MX35.2, MX49.2, MX5.2, MX63.2
- new net col5: MX21.2, MX36.2, MX50.2, MX6.2, MX64.2
- new net col6: MX22.2, MX37.2, MX51.2, MX65.2, MX7.2, MX77.2
- new net col7: MX23.2, MX38.2, MX52.2, MX66.2, MX8.2
- new net col8: MX24.2, MX39.2, MX53.2, MX67.2, MX9.2
- new net col9: MX10.2, MX25.2, MX40.2, MX54.2, MX68.2, MX78.2
- new net row0: D10.1 (K), D11.1 (K), D12.1 (K), D13.1 (K), D14.1 (K), D15.1 (K), D16.1 (K), D2.1 (K), D3.1 (K), D4.1 (K), D5.1 (K), D6.1 (K), D7.1 (K), D8.1 (K), D9.1 (K)
- new net row1: D17.1 (K), D18.1 (K), D19.1 (K), D20.1 (K), D21.1 (K), D22.1 (K), D23.1 (K), D24.1 (K), D25.1 (K), D26.1 (K), D27.1 (K), D28.1 (K), D29.1 (K), D30.1 (K), D31.1 (K)
- new net row2: D32.1 (K), D33.1 (K), D34.1 (K), D35.1 (K), D36.1 (K), D37.1 (K), D38.1 (K), D39.1 (K), D40.1 (K), D41.1 (K), D42.1 (K), D43.1 (K), D44.1 (K), D45.1 (K), D46.1 (K)
- new net row3: D47.1 (K), D48.1 (K), D49.1 (K), D50.1 (K), D51.1 (K), D52.1 (K), D53.1 (K), D54.1 (K), D55.1 (K), D56.1 (K), D57.1 (K), D58.1 (K), D59.1 (K), D60.1 (K)
- new net row4: D61.1 (K), D62.1 (K), D63.1 (K), D64.1 (K), D65.1 (K), D66.1 (K), D67.1 (K), D68.1 (K), D69.1 (K), D70.1 (K), D71.1 (K), D72.1 (K), D73.1 (K), D74.1 (K)
- new net row5: D75.1 (K), D76.1 (K), D77.1 (K), D78.1 (K), D79.1 (K), D80.1 (K), D81.1 (K), D82.1 (K), D83.1 (K), D84.1 (K)
